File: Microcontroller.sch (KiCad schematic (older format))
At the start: 28 parts, among them J1 USB, K1 CONN_3, K2 CONN_3, P23 CONN_1, U3 PIC18F4550, U4 FT230X, X1 4MHz

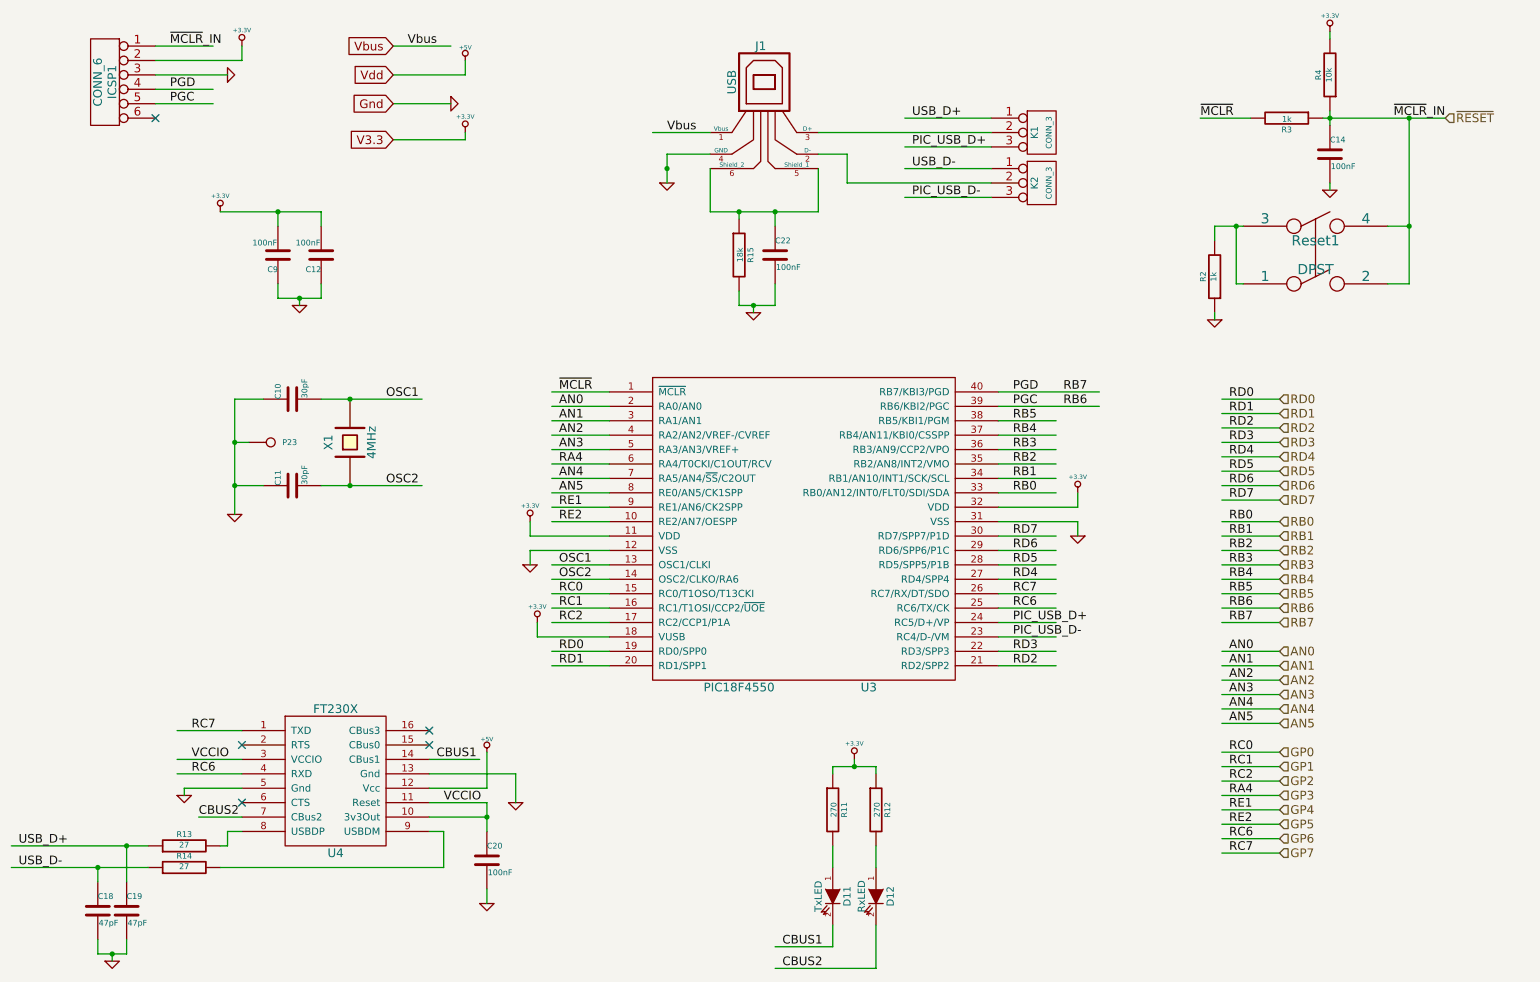
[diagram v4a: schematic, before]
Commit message: This branch uses a MCP2200 rather than an FTDI chip
Signed-off-by: Kolijn Wolfaardt <kolijn.wolfaardt@gmail.com>
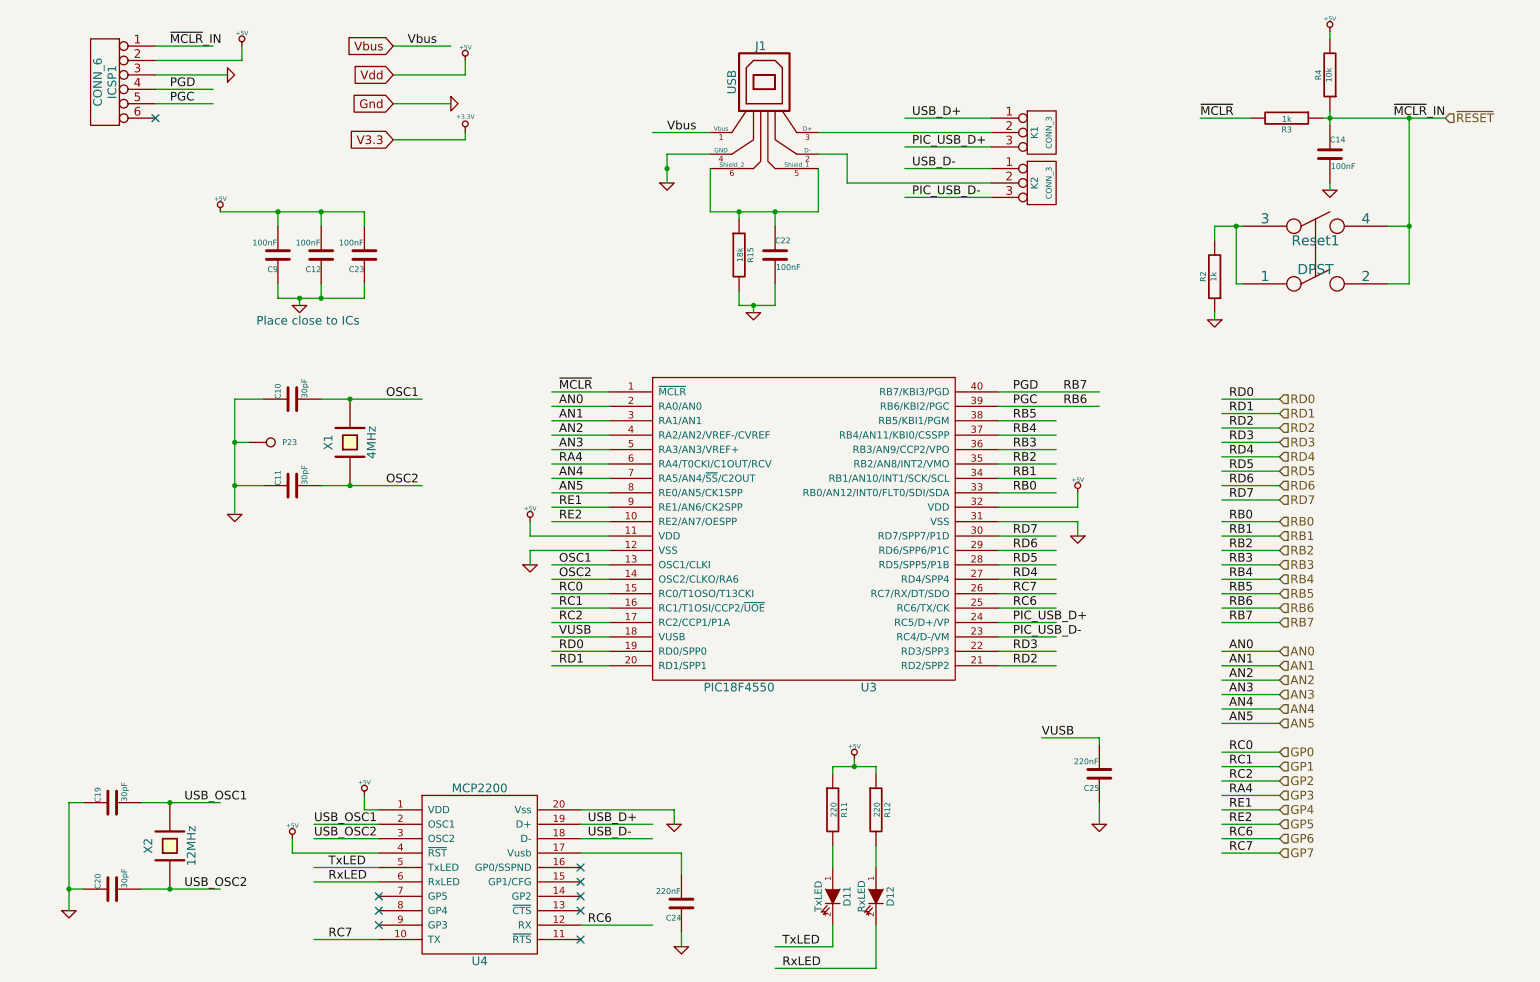
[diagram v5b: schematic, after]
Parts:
- removed C18: 47pF, ~, symbol C
- removed R13, R14: 27, ~, symbol R
- removed U4: FT230X, ~, symbol FT230X
- added C23: 100nF, ~, symbol C
- added C24, C25: 220nF, ~, symbol C
- added U4: MCP2200, ~, symbol MCP2200
- added X2: 12MHz, ~, symbol CRYSTAL
- C19: value 47pF -> 30pF
- C20: value 100nF -> 30pF
- R11, R12: value 270 -> 220
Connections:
- net labels added: RxLED, TxLED, USB_OSC1, USB_OSC2, VUSB
- net labels removed: CBUS1, CBUS2, VCCIO
- wire segments 172 -> 169
- no-connect marks 5 -> 9
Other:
- note added: "Place close to ICs"

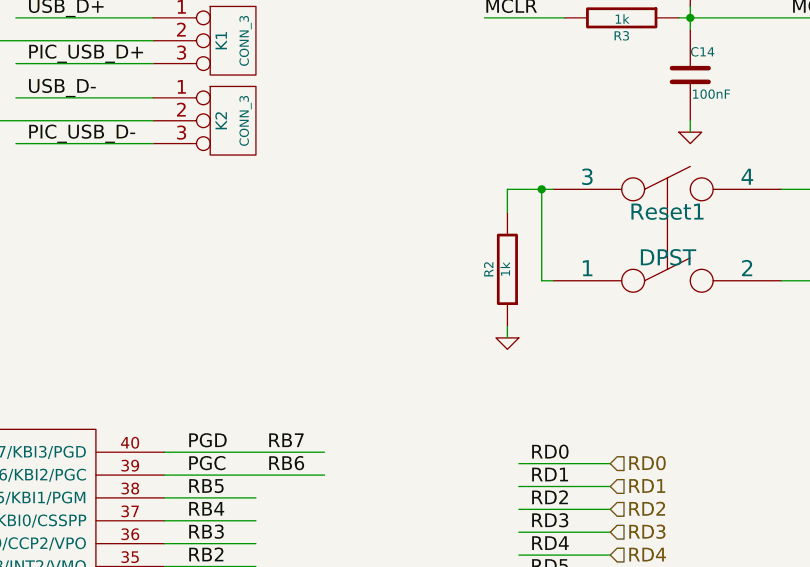
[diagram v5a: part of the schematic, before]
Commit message: Replace resistor R2 with a 0Ohm
Signed-off-by: Kolijn Wolfaardt <kolijn.wolfaardt@gmail.com>
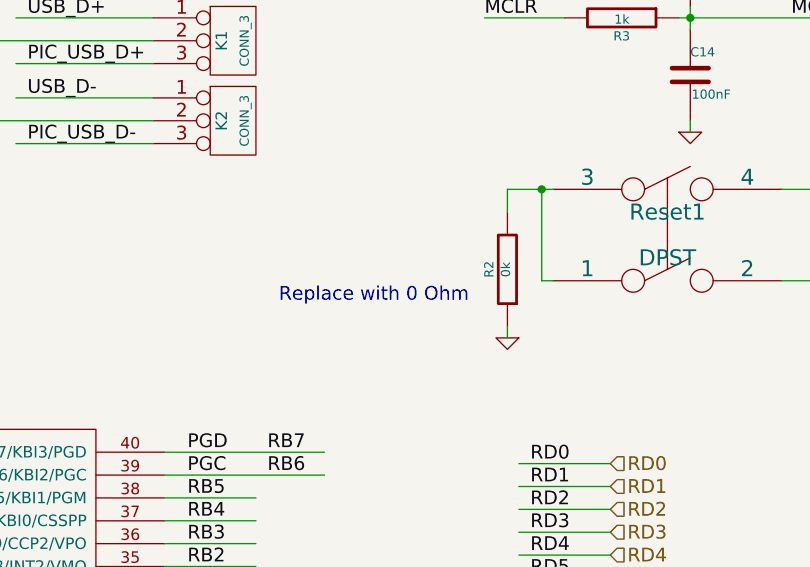
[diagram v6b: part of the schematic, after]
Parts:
- R2: value 1k -> 0k
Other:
- note added: "Replace with 0 Ohm"
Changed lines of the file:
@@
 Sheet 4 6
 Title ""
-Date "20 apr 2014"
+Date "20 jul 2014"
 Rev ""
 Comp ""
@@
 P 9050 2600
 F 0 "R2" V 9130 2600 40  0000 C CNN
-F 1 "1k" V 9057 2601 40  0000 C CNN
+F 1 "0k" V 9057 2601 40  0000 C CNN
 F 2 "~" V 8980 2600 30  0000 C CNN
 F 3 "~" H 9050 2600 30  0000 C CNN
@@
 	1    0    0    -1
 $EndComp
+Text Notes 8050 2750 0    60   ~ 0
+Replace with 0 Ohm
 $EndSCHEMATC
